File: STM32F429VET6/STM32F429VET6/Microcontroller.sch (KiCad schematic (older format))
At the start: 3 parts

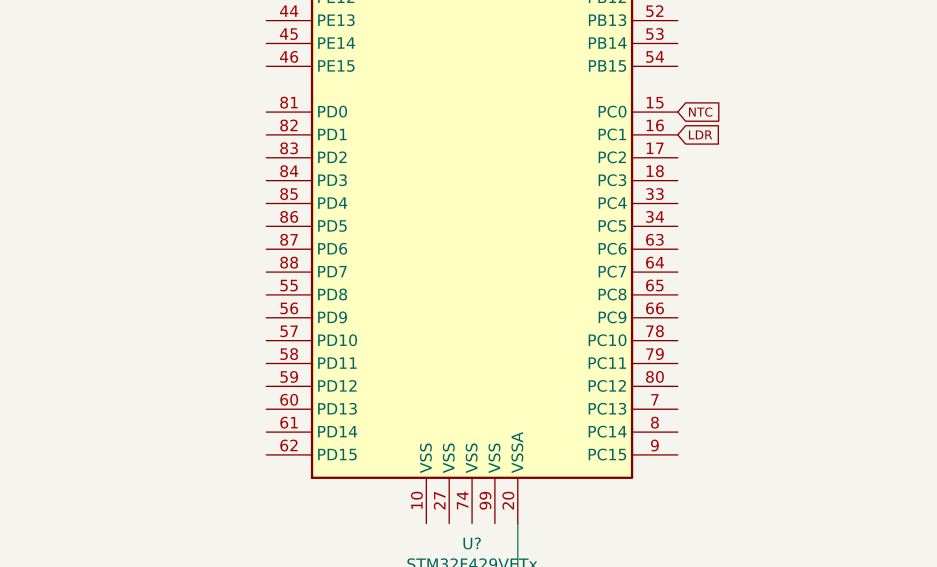
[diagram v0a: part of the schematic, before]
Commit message: Started adding pin classification
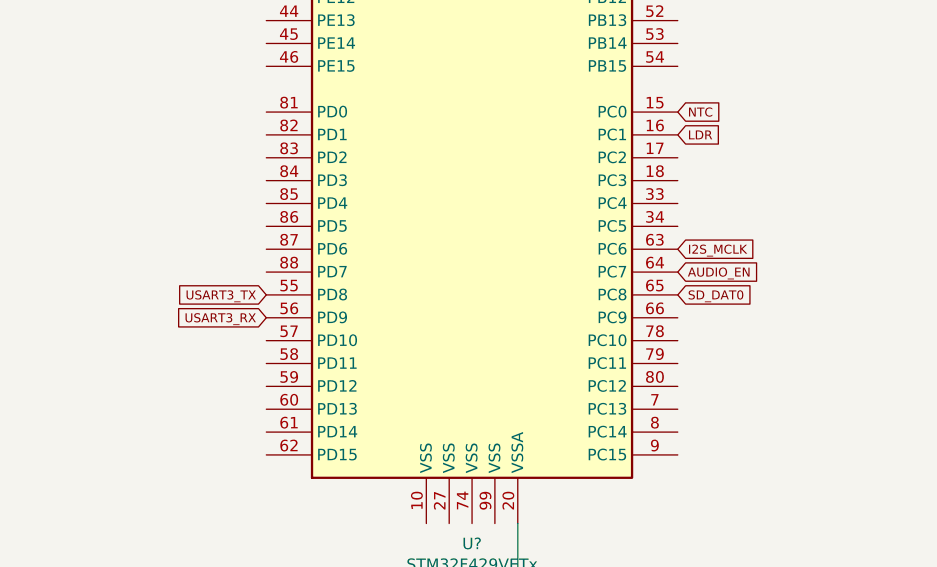
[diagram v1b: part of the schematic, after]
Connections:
- net USART3_TX: now reaches U?.55 (PD8)
- net USART3_RX: now reaches U?.56 (PD9)
- net I2S_MCLK: now reaches U?.63 (PC6)
- net AUDIO_EN: now reaches U?.64 (PC7)
- net SD_DAT0: now reaches U?.65 (PC8)
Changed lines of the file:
@@
 EESchema Schematic File Version 4
+LIBS:STM32F429VET6-cache
 EELAYER 29 0
 EELAYER END
@@
 Wire Wire Line
 	4500 7050 4500 6750
+Text GLabel 5200 5550 2    39   Input ~ 0
+I2S_MCLK
+Text GLabel 5200 5650 2    39   Input ~ 0
+AUDIO_EN
+Text GLabel 5200 5750 2    39   Input ~ 0
+SD_DAT0
+Text GLabel 3400 5750 0    39   Input ~ 0
+USART3_TX
+Text GLabel 3400 5850 0    39   Input ~ 0
+USART3_RX
 $EndSCHEMATC

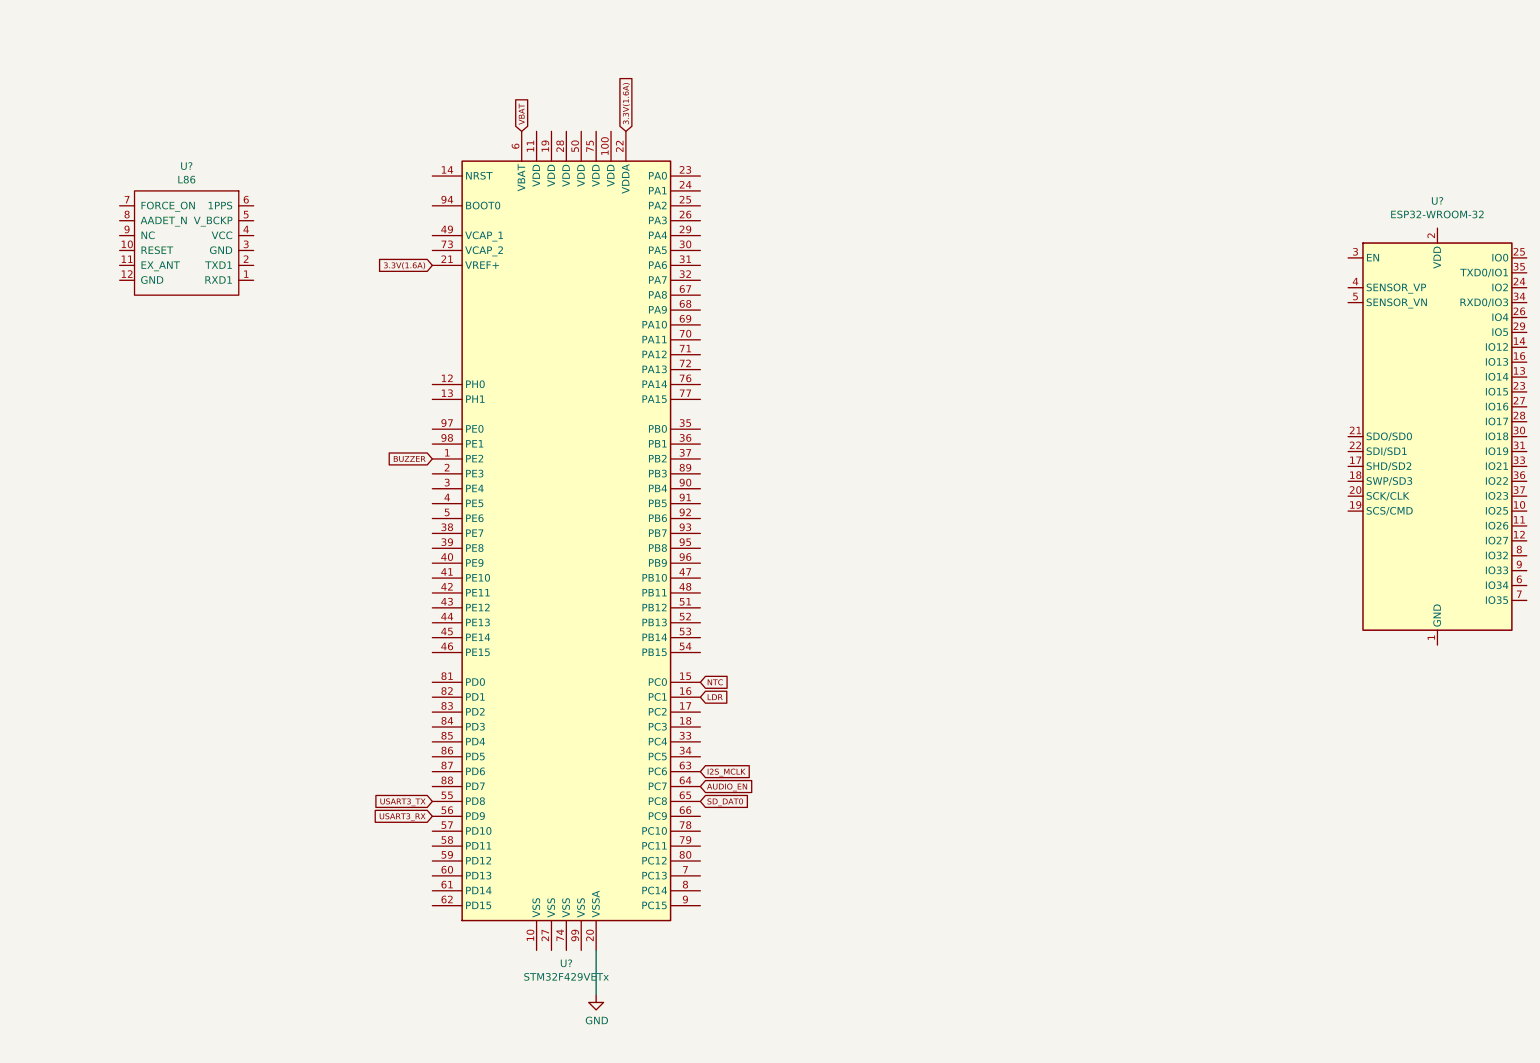
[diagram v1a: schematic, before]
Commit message: Completed Microcontroller part
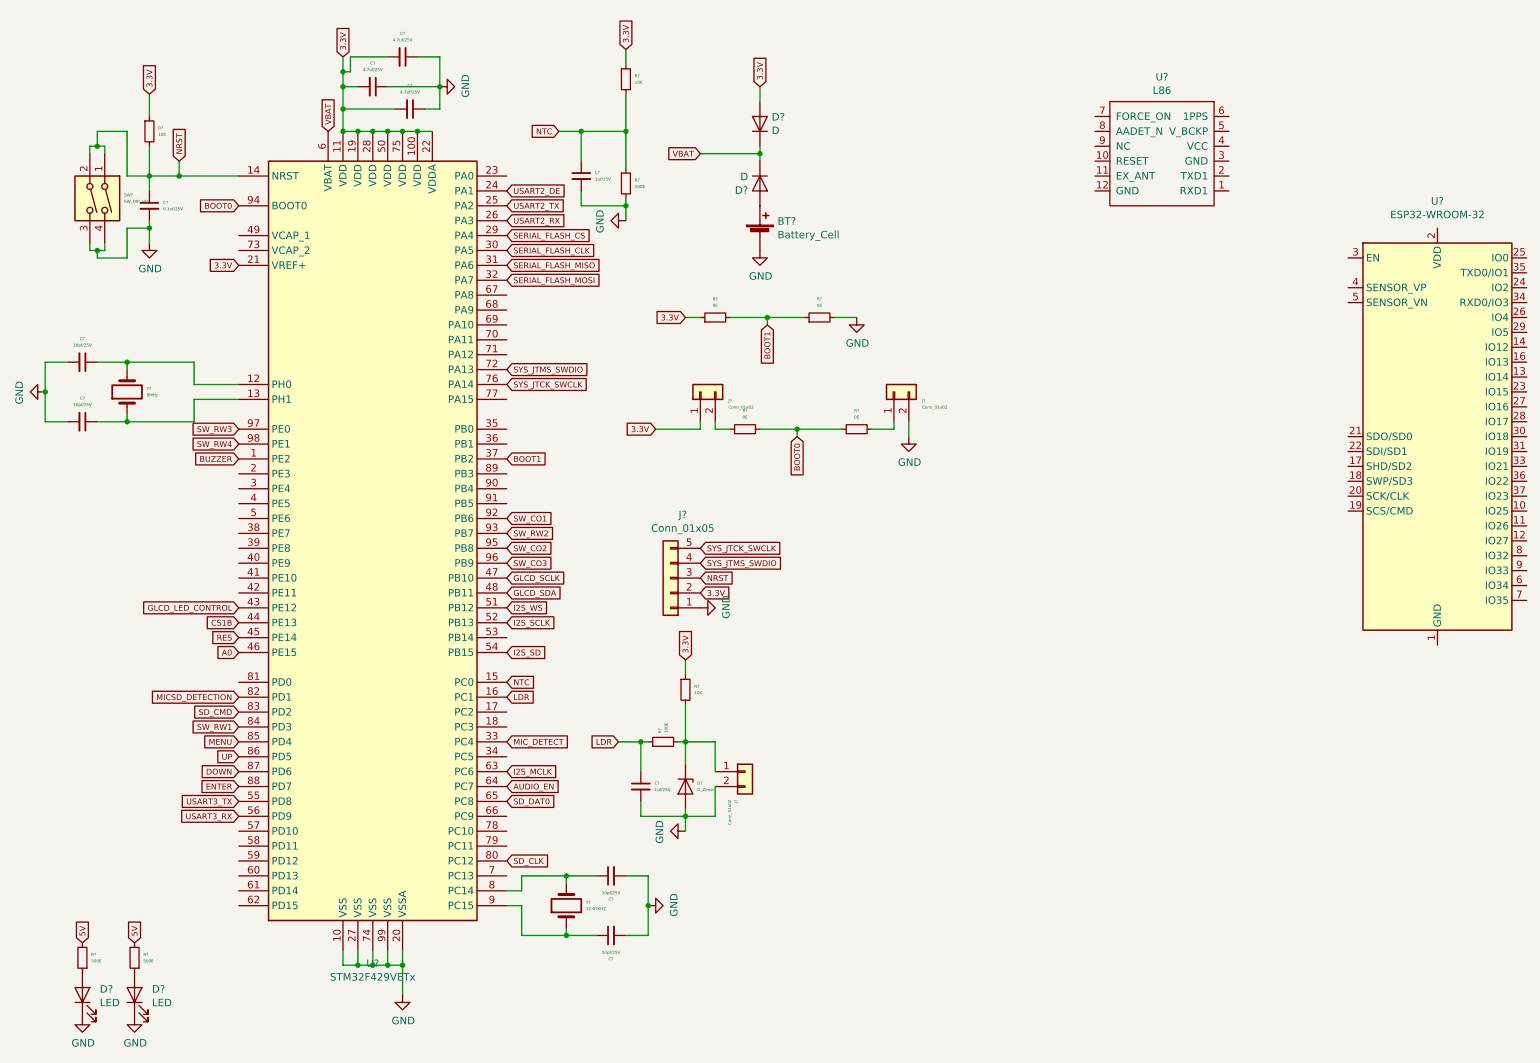
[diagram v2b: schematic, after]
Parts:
- added BT?: Battery_Cell, symbol Device:Battery_Cell
- added C? (x3): 4.7uf/25V, symbol Device:C_Small
- added C? (x4): 10pf/25V, symbol Device:C_Small
- added C?: 0.1uf/25V, symbol Device:C_Small
- added C? (x2): 1uf/25V, symbol Device:C_Small
- added D? (x2): LED, LED_SMD:LED_0805_2012Metric_Pad1.15x1.40mm_HandSolder, symbol Device:LED
- added D?: D_Zener, symbol Device:D_Zener
- added D? (x2): D, symbol Device:D
- added J? (x3): Conn_01x02, Connector_PinHeader_2.54mm:PinHeader_1x02_P2.54mm_Vertical, symbol Connector_Generic:Conn_01x02
- added J?: Conn_01x05, Connector_PinHeader_2.54mm:PinHeader_1x05_P2.54mm_Vertical, symbol Connector_Generic:Conn_01x05
- added R?: 10K, symbol Device:R_Small
- added R? (x4): 0E, Resistor_SMD:R_0805_2012Metric_Pad1.15x1.40mm_HandSolder, symbol Device:R_Small
- added R? (x2): 10K, Resistor_SMD:R_0805_2012Metric_Pad1.15x1.40mm_HandSolder, symbol Device:R_Small
- added R? (x2): 100E, Resistor_SMD:R_0805_2012Metric_Pad1.15x1.40mm_HandSolder, symbol Device:R_Small
- added R? (x2): 500E, Resistor_SMD:R_0805_2012Metric_Pad1.15x1.40mm_HandSolder, symbol Device:R_Small
- added SW?: SW_DIP_x02, symbol Switch:SW_DIP_x02
- added Y?: 8MHz, symbol Device:Crystal
- added Y?: 32.67KHZ, symbol Device:Crystal
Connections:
- net 3.3V(1.6A) is gone; now on net 3.3V: U?.21 (VREF+), U?.22 (VDDA)
- net GND: now also U?.10 (VSS), U?.27 (VSS), U?.74 (VSS), U?.99 (VSS), BT?.2 (-), C?.1, C?.1, C?.1, C?.2, C?.2, C?.2, C?.2, C?.2, C?.2, C?.2, D?.1 (K), D?.1 (K), D?.2 (A), J?.1 (Pin_1), J?.2 (Pin_2), J?.2 (Pin_2), R?.2, R?.2, SW?.3, SW?.4
- net LDR: now also C?.1, R?.1
- net NTC: now also C?.1, R?.1, R?.2
- net VBAT: now also D?.1 (K), D?.1 (K)
- net 3.3V: now reaches U?.100 (VDD)
- net 3.3V: now also U?.11 (VDD), U?.19 (VDD), U?.28 (VDD), U?.50 (VDD), U?.75 (VDD), C?.2, C?.2, C?.2, D?.2 (A), J?.1 (Pin_1), J?.2 (Pin_2), R?.1, R?.1, R?.1, R?.1
- net at U?.12 (PH0): now also C?.1, Y?.2
- net at U?.13 (PH1): now also C?.1, Y?.1
- net NRST: now reaches U?.14 (NRST)
- net NRST: now also C?.1, J?.3 (Pin_3), R?.2, SW?.1, SW?.2
- net USART2_DE: now reaches U?.24 (PA1)
- net USART2_TX: now reaches U?.25 (PA2)
- net USART2_RX: now reaches U?.26 (PA3)
- net SERIAL_FLASH_CS: now reaches U?.29 (PA4)
- net SERIAL_FLASH_CLK: now reaches U?.30 (PA5)
- net SERIAL_FLASH_MISO: now reaches U?.31 (PA6)
- net SERIAL_FLASH_MOSI: now reaches U?.32 (PA7)
- net MIC_DETECT: now reaches U?.33 (PC4)
- net BOOT1: now reaches U?.37 (PB2)
- net BOOT1: now also R?.1, R?.2
- net GLCD_LED_CONTROL: now reaches U?.43 (PE12)
- net CS1B: now reaches U?.44 (PE13)
- net RES: now reaches U?.45 (PE14)
- net A0: now reaches U?.46 (PE15)
- net GLCD_SCLK: now reaches U?.47 (PB10)
- net GLCD_SDA: now reaches U?.48 (PB11)
- net I2S_WS: now reaches U?.51 (PB12)
- net I2S_SCLK: now reaches U?.52 (PB13)
- net I2S_SD: now reaches U?.54 (PB15)
- net SYS_JTMS_SWDIO: now reaches U?.72 (PA13)
- net SYS_JTMS_SWDIO: now also J?.4 (Pin_4)
- net SYS_JTCK_SWCLK: now reaches U?.76 (PA14)
- net SYS_JTCK_SWCLK: now also J?.5 (Pin_5)
- net at U?.8 (PC14): now also C?.1, Y?.2
- net SD_CLK: now reaches U?.80 (PC12)
- net MICSD_DETECTION: now reaches U?.82 (PD1)
- net SD_CMD: now reaches U?.83 (PD2)
- net SW_RW1: now reaches U?.84 (PD3)
- net MENU: now reaches U?.85 (PD4)
- net UP: now reaches U?.86 (PD5)
- net DOWN: now reaches U?.87 (PD6)
- net ENTER: now reaches U?.88 (PD7)
- net at U?.9 (PC15): now also C?.1, Y?.1
- net SW_CO1: now reaches U?.92 (PB6)
- net SW_RW2: now reaches U?.93 (PB7)
- net BOOT0: now reaches U?.94 (BOOT0)
- net BOOT0: now also R?.1, R?.2
- net SW_CO2: now reaches U?.95 (PB8)
- net SW_CO3: now reaches U?.96 (PB9)
- net SW_RW3: now reaches U?.97 (PE0)
- net SW_RW4: now reaches U?.98 (PE1)
- new net: J?.2 (Pin_2), R?.1
- new net: J?.1 (Pin_1), R?.2
- new net: D?.2 (A), R?.1 (x2)
- new net: D?.1 (K), J?.1 (Pin_1), R?.2, R?.2
- new net: BT?.1 (+), D?.2 (A)
- new net 5V: R?.2, R?.2
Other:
- moved on the sheet: U?

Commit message: Initial Completion of the PDF
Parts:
- removed D? (x2): D, symbol Device:D
- added D? (x2): T4, Diode_SMD:D_SOD-123, symbol Diode:1N4148W
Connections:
- net 3.3V: now also D?.2 (A)
- net VBAT: now also D?.1 (K), D?.1 (K)
- net at BT?.1 (+): now also D?.2 (A)
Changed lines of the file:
@@
 Text GLabel 5600 950  1    39   Input ~ 0
 3.3V
-$Comp
-L Device:D D?
-U 1 1 5FE420F1
-P 5600 1200
-F 0 "D?" V 5646 1121 50  0000 R CNN
-F 1 "D" V 5555 1121 50  0000 R CNN
-F 2 "" H 5600 1200 50  0001 C CNN
-F 3 "~" H 5600 1200 50  0001 C CNN
-	1    5600 1200
-	0    -1   -1   0
-$EndComp
-$Comp
-L Device:D D?
-U 1 1 5FE429DA
-P 5600 1600
-F 0 "D?" V 5646 1521 50  0000 R CNN
-F 1 "D" V 5555 1521 50  0000 R CNN
-F 2 "" H 5600 1600 50  0001 C CNN
-F 3 "~" H 5600 1600 50  0001 C CNN
-	1    5600 1600
-	0    1    1    0
-$EndComp
 Wire Wire Line
 	5600 1450 5600 1400
@@
 Wire Wire Line
 	4000 6250 4300 6250
+$Comp
+L Diode:1N4148W D?
+U 1 1 606285B0
+P 5600 1200
+AR Path="/5FE8625C/606285B0" Ref="D?"  Part="1"
+AR Path="/5FD5E119/606285B0" Ref="D?"  Part="1"
+F 0 "D?" V 5554 1280 50  0000 L CNN
+F 1 "T4" V 5645 1280 50  0000 L CNN
+F 2 "Diode_SMD:D_SOD-123" H 5600 1025 50  0001 C CNN
+F 3 "https://www.vishay.com/docs/85748/1n4148w.pdf" H 5600 1200 50  0001 C CNN
+	1    5600 1200
+	0    -1   -1   0
+$EndComp
+$Comp
+L Diode:1N4148W D?
+U 1 1 60633318
+P 5600 1600
+AR Path="/5FE8625C/60633318" Ref="D?"  Part="1"
+AR Path="/5FD5E119/60633318" Ref="D?"  Part="1"
+F 0 "D?" V 5554 1680 50  0000 L CNN
+F 1 "T4" V 5645 1680 50  0000 L CNN
+F 2 "Diode_SMD:D_SOD-123" H 5600 1425 50  0001 C CNN
+F 3 "https://www.vishay.com/docs/85748/1n4148w.pdf" H 5600 1600 50  0001 C CNN
+	1    5600 1600
+	0    1    1    0
+$EndComp
 $EndSCHEMATC

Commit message: Started working on the ESP32 connection
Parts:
- removed U?: ESP32-WROOM-32, RF_Module:ESP32-WROOM-32, symbol RF_Module:ESP32-WROOM-32
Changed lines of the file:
@@
 $Descr A4 11693 8268
 encoding utf-8
-Sheet 2 3
+Sheet 2 4
 Title ""
 Date ""
@@
 Comment4 ""
 $EndDescr
-$Comp
-L RF_Module:ESP32-WROOM-32 U?
-U 1 1 5FD62675
-P 10150 3300
-AR Path="/5FD62675" Ref="U?"  Part="1"
-AR Path="/5FD5E119/5FD62675" Ref="U?"  Part="1"
-F 0 "U?" H 10150 4881 50  0000 C CNN
-F 1 "ESP32-WROOM-32" H 10150 4790 50  0000 C CNN
-F 2 "RF_Module:ESP32-WROOM-32" H 10150 1800 50  0001 C CNN
-F 3 "https://www.espressif.com/sites/default/files/documentation/esp32-wroom-32_datasheet_en.pdf" H 9850 3350 50  0001 C CNN
-	1    10150 3300
-	1    0    0    -1
-$EndComp
 $Comp
 L Quectel_L86:L86 U?
@@
 	0    1    1    0
 $EndComp
+$Sheet
+S 8500 5100 1800 950
+U 60922ED4
+F0 "ESP32-WROOM-32" 39
+F1 "ESP32-WROOM-32.sch" 39
+$EndSheet
 $EndSCHEMATC

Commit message: Completed ESP32 connection
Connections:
- net UART2_TX(ESP): now reaches U?.38 (PE7)
- net UART2_RX(ESP): now reaches U?.39 (PE8)
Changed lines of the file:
@@
 F1 "ESP32-WROOM-32.sch" 39
 $EndSheet
+Text GLabel 7550 4450 2    39   Input ~ 0
+UART2_RX(ESP)
+Text GLabel 7550 4550 2    39   Input ~ 0
+UART2_TX(ESP)
+Text GLabel 2100 3950 0    39   Input ~ 0
+UART7_RX
+Text GLabel 2100 4050 0    39   Input ~ 0
+UART7_TX
+Text GLabel 7300 4550 0    39   Input ~ 0
+UART7_RX
+Text GLabel 7300 4450 0    39   Input ~ 0
+UART7_TX
+Wire Wire Line
+	7550 4450 7300 4450
+Wire Wire Line
+	7300 4550 7550 4550
 $EndSCHEMATC
